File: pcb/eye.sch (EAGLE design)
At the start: 89 parts, among them J2 JST-ZH-5SMD-RA, Q1 ECS-160-20-3X-TR, U1 WS2812, U10 WS2812, U11 WS2812, U12 WS2812, U13 WS2812, U14 WS2812, U15 WS2812, U16 WS2812, U17 WS2812, U18 WS2812, U19 WS2812, U2 WS2812, U20 WS2812, U21 WS2812, U22 WS2812, U23 WS2812, U24 WS2812, U25 WS2812, U26 WS2812, U27 WS2812, U28 WS2812, U29 WS2812, U3 WS2812, U30 WS2812, U31 WS2812, U32 WS2812, U33 WS2812, U34 WS2812, U35 WS2812, U36 WS2812, U37 WS2812, U38 WS2812, U39 WS2812, U4 WS2812, U40 WS2812, U41 WS2812, U42 WS2812, U43 WS2812, U44 WS2812, U45 WS2812, U46 WS2812, U47 WS2812, U48 WS2812, U49 WS2812, U5 WS2812, U50 WS2812, U51 WS2812, U52 WS2812, U53 WS2812, U54 WS2812, U55 WS2812, U56 WS2812, U57 WS2812, U58 WS2812, U59 WS2812, U6 WS2812, U60 WS2812, U7 WS2812, U8 WS2812, U9 WS2812

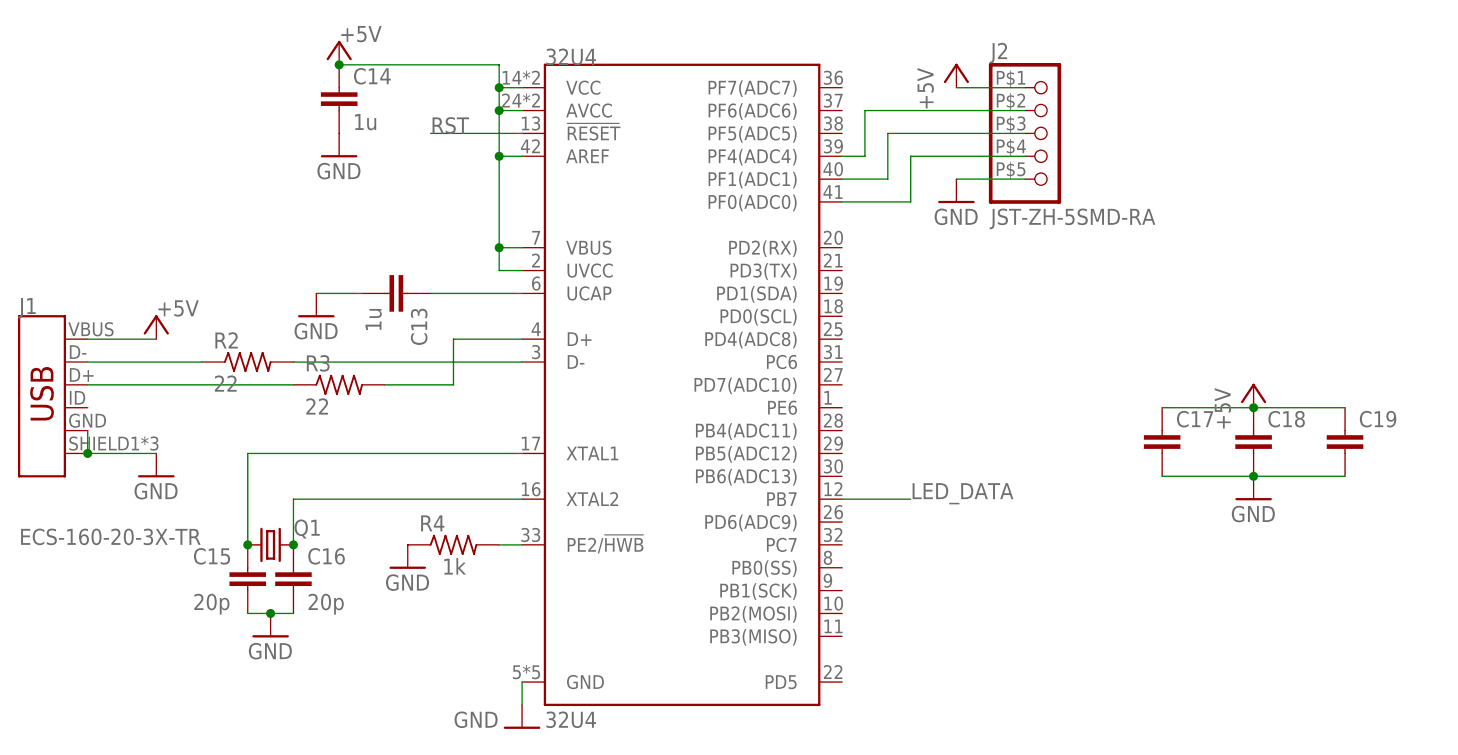
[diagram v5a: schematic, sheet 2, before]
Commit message: touch up silkscreen and traces
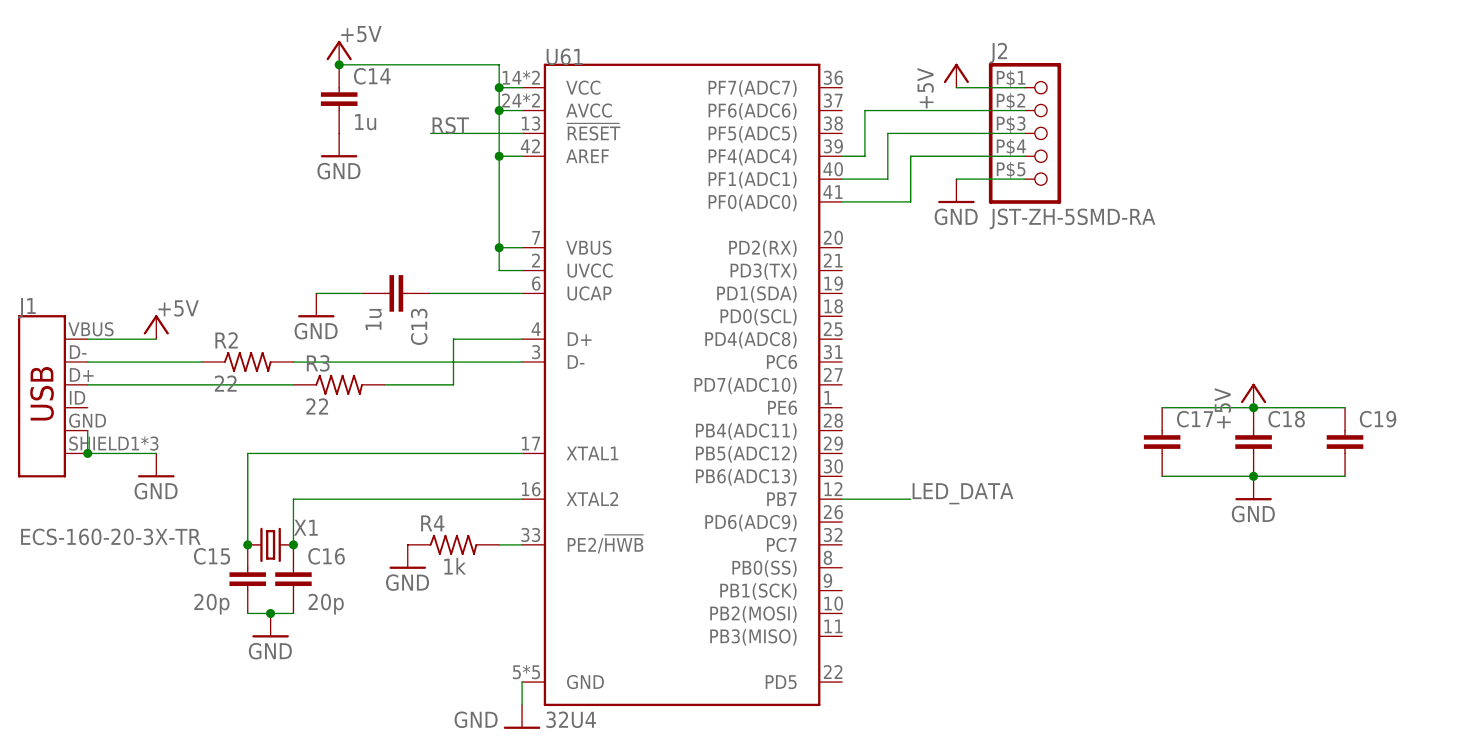
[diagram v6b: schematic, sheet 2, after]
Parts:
- renumbered 32U4 to U61, Q1 to X1
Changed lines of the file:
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@@
 <part name="R4" library="rcl" library_urn="urn:adsk.eagle:library:334" deviceset="R-US_" device="R0603" package3d_urn="urn:adsk.eagle:package:23555/3" value="1k"/>
 <part name="GND78" library="supply1" library_urn="urn:adsk.eagle:library:371" deviceset="GND" device=""/>
-<part name="Q1" library="SparkFun-Clocks" deviceset="CRYSTAL" device="SMD-3.2X1.5" value="ECS-160-20-3X-TR"/>
+<part name="X1" library="SparkFun-Clocks" deviceset="CRYSTAL" device="SMD-3.2X1.5" value="ECS-160-20-3X-TR"/>
 <part name="C15" library="rcl" library_urn="urn:adsk.eagle:library:334" deviceset="C-EU" device="C0603" package3d_urn="urn:adsk.eagle:package:23616/2" value="20p"/>
 <part name="C16" library="rcl" library_urn="urn:adsk.eagle:library:334" deviceset="C-EU" device="C0603" package3d_urn="urn:adsk.eagle:package:23616/2" value="20p"/>
 <part name="GND79" library="supply1" library_urn="urn:adsk.eagle:library:371" deviceset="GND" device=""/>
-<part name="32U4" library="SparkFun-IC-Microcontroller" deviceset="ATMEGA32U4" device="QFN" value="32U4"/>
+<part name="U61" library="SparkFun-IC-Microcontroller" deviceset="ATMEGA32U4" device="QFN" value="32U4"/>
 <part name="P+37" library="supply1" library_urn="urn:adsk.eagle:library:371" deviceset="+5V" device=""/>
 <part name="GND37" library="supply1" library_urn="urn:adsk.eagle:library:371" deviceset="GND" device=""/>
@@
 <attribute name="VALUE" x="40.64" y="30.48" size="1.778" layer="96"/>
 </instance>
-<instance part="Q1" gate="G$1" x="27.94" y="35.56" smashed="yes">
+<instance part="X1" gate="G$1" x="27.94" y="35.56" smashed="yes">
 <attribute name="NAME" x="30.48" y="36.576" size="1.778" layer="95"/>
 <attribute name="VALUE" x="0" y="35.56" size="1.778" layer="96"/>
@@
 <attribute name="VALUE" x="25.4" y="22.86" size="1.778" layer="96"/>
 </instance>
-<instance part="32U4" gate="U1" x="73.66" y="55.88" smashed="yes">
+<instance part="U61" gate="U1" x="73.66" y="55.88" smashed="yes">
 <attribute name="NAME" x="58.42" y="88.9" size="1.778" layer="95"/>
 <attribute name="VALUE" x="58.42" y="15.24" size="1.778" layer="96"/>
@@
 <pinref part="C14" gate="G$1" pin="1"/>
 <junction x="35.56" y="88.9"/>
-<pinref part="32U4" gate="U1" pin="VCC@14"/>
+<pinref part="U61" gate="U1" pin="VCC@14"/>
 <wire x1="53.34" y1="86.36" x2="53.34" y2="83.82" width="0.1524" layer="91"/>
 <wire x1="53.34" y1="83.82" x2="53.34" y2="78.74" width="0.1524" layer="91"/>
@@
 <wire x1="55.88" y1="86.36" x2="53.34" y2="86.36" width="0.1524" layer="91"/>
 <junction x="53.34" y="86.36"/>
-<pinref part="32U4" gate="U1" pin="AVCC@24"/>
+<pinref part="U61" gate="U1" pin="AVCC@24"/>
 <wire x1="55.88" y1="83.82" x2="53.34" y2="83.82" width="0.1524" layer="91"/>
 <junction x="53.34" y="83.82"/>
-<pinref part="32U4" gate="U1" pin="AREF"/>
+<pinref part="U61" gate="U1" pin="AREF"/>
 <wire x1="55.88" y1="78.74" x2="53.34" y2="78.74" width="0.1524" layer="91"/>
 <junction x="53.34" y="78.74"/>
-<pinref part="32U4" gate="U1" pin="VBUS"/>
+<pinref part="U61" gate="U1" pin="VBUS"/>
 <wire x1="55.88" y1="68.58" x2="53.34" y2="68.58" width="0.1524" layer="91"/>
 <junction x="53.34" y="68.58"/>
-<pinref part="32U4" gate="U1" pin="UVCC"/>
+<pinref part="U61" gate="U1" pin="UVCC"/>
 <wire x1="55.88" y1="66.04" x2="53.34" y2="66.04" width="0.1524" layer="91"/>
 </segment>
@@
 <wire x1="55.88" y1="20.32" x2="55.88" y2="17.78" width="0.1524" layer="91"/>
 <pinref part="GND77" gate="1" pin="GND"/>
-<pinref part="32U4" gate="U1" pin="GND"/>
+<pinref part="U61" gate="U1" pin="GND"/>
 </segment>
 <segment>
@@
 <pinref part="C13" gate="G$1" pin="1"/>
 <wire x1="55.88" y1="63.5" x2="45.72" y2="63.5" width="0.1524" layer="91"/>
-<pinref part="32U4" gate="U1" pin="UCAP"/>
+<pinref part="U61" gate="U1" pin="UCAP"/>
 </segment>
 </net>
@@
 <wire x1="48.26" y1="53.34" x2="48.26" y2="58.42" width="0.1524" layer="91"/>
 <wire x1="48.26" y1="58.42" x2="55.88" y2="58.42" width="0.1524" layer="91"/>
-<pinref part="32U4" gate="U1" pin="D+"/>
+<pinref part="U61" gate="U1" pin="D+"/>
 </segment>
 </net>
@@
 <pinref part="R2" gate="G$1" pin="2"/>
 <wire x1="30.48" y1="55.88" x2="55.88" y2="55.88" width="0.1524" layer="91"/>
-<pinref part="32U4" gate="U1" pin="D-"/>
+<pinref part="U61" gate="U1" pin="D-"/>
 </segment>
 </net>
 <net name="N$67" class="0">
 <segment>
-<pinref part="Q1" gate="G$1" pin="2"/>
+<pinref part="X1" gate="G$1" pin="2"/>
 <wire x1="30.48" y1="35.56" x2="30.48" y2="40.64" width="0.1524" layer="91"/>
 <wire x1="30.48" y1="40.64" x2="55.88" y2="40.64" width="0.1524" layer="91"/>
 <pinref part="C16" gate="G$1" pin="1"/>
 <junction x="30.48" y="35.56"/>
-<pinref part="32U4" gate="U1" pin="XTAL2"/>
+<pinref part="U61" gate="U1" pin="XTAL2"/>
 </segment>
 </net>
 <net name="N$68" class="0">
 <segment>
-<pinref part="Q1" gate="G$1" pin="1"/>
+<pinref part="X1" gate="G$1" pin="1"/>
 <wire x1="25.4" y1="35.56" x2="25.4" y2="45.72" width="0.1524" layer="91"/>
 <wire x1="25.4" y1="45.72" x2="55.88" y2="45.72" width="0.1524" layer="91"/>
 <pinref part="C15" gate="G$1" pin="1"/>
 <junction x="25.4" y="35.56"/>
-<pinref part="32U4" gate="U1" pin="XTAL1"/>
+<pinref part="U61" gate="U1" pin="XTAL1"/>
 </segment>
 </net>
@@
 <wire x1="55.88" y1="81.28" x2="45.72" y2="81.28" width="0.1524" layer="91"/>
 <label x="45.72" y="81.28" size="1.778" layer="95"/>
-<pinref part="32U4" gate="U1" pin="!RESET"/>
+<pinref part="U61" gate="U1" pin="!RESET"/>
 </segment>
 </net>
@@
 <segment>
 <pinref part="R4" gate="G$1" pin="2"/>
-<pinref part="32U4" gate="U1" pin="PE2/!HWB"/>
+<pinref part="U61" gate="U1" pin="PE2/!HWB"/>
 <wire x1="53.34" y1="35.56" x2="55.88" y2="35.56" width="0.1524" layer="91"/>
 </segment>
@@
 <net name="LED_DATA" class="0">
 <segment>
-<pinref part="32U4" gate="U1" pin="PB7"/>
+<pinref part="U61" gate="U1" pin="PB7"/>
 <wire x1="91.44" y1="40.64" x2="99.06" y2="40.64" width="0.1524" layer="91"/>
 <label x="99.06" y="40.64" size="1.778" layer="95"/>
@@
 <net name="N$30" class="0">
 <segment>
-<pinref part="32U4" gate="U1" pin="PF0(ADC0)"/>
+<pinref part="U61" gate="U1" pin="PF0(ADC0)"/>
 <wire x1="91.44" y1="73.66" x2="99.06" y2="73.66" width="0.1524" layer="91"/>
 <pinref part="J2" gate="G$1" pin="4"/>
@@
 <net name="N$63" class="0">
 <segment>
-<pinref part="32U4" gate="U1" pin="PF1(ADC1)"/>
+<pinref part="U61" gate="U1" pin="PF1(ADC1)"/>
 <wire x1="91.44" y1="76.2" x2="96.52" y2="76.2" width="0.1524" layer="91"/>
 <wire x1="96.52" y1="76.2" x2="96.52" y2="81.28" width="0.1524" layer="91"/>
@@
 <net name="N$64" class="0">
 <segment>
-<pinref part="32U4" gate="U1" pin="PF4(ADC4)"/>
+<pinref part="U61" gate="U1" pin="PF4(ADC4)"/>
 <wire x1="91.44" y1="78.74" x2="93.98" y2="78.74" width="0.1524" layer="91"/>
 <pinref part="J2" gate="G$1" pin="2"/>

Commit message: optimize some routing
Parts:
- added S1: MOMENTARY-SWITCH-SPST-SMD-6.0X3.5MM, SparkFun-Switches:MOMENTARY-SWITCH-SPST-SMD-6.0X3.5MM
- X1: device SparkFun-Clocks:CRYSTALSMD-3.2X1.5 -> SparkFun-Clocks:CRYSTALSMD-5X3.2-2PAD
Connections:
- net GND: now also S1.1
- net RST: now also S1.2

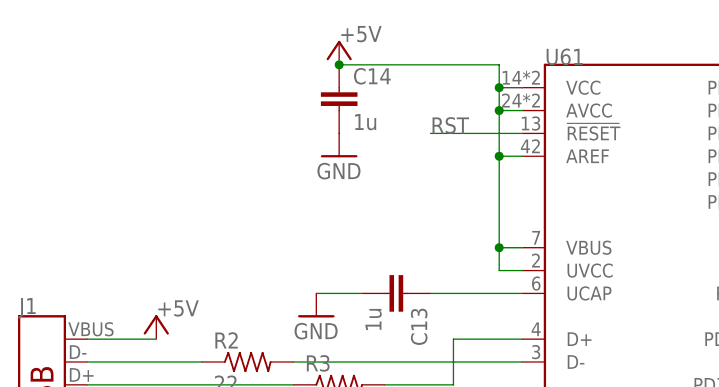
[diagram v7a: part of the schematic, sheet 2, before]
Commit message: add 10uF VBUS cap
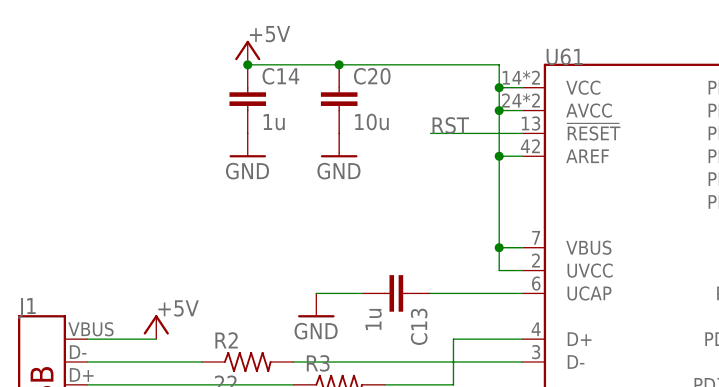
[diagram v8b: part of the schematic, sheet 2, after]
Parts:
- added C20: 10u, rcl:C-EUC0603
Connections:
- net +5V: now also C20.1
- net GND: now also C20.2
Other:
- moved on the sheet: C14
